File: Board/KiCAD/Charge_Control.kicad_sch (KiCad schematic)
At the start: 57 parts, among them Q1 AON7408, Q10 AON7407, Q2 AON7408, Q3 AON7408, Q4 AON7408, U1 BQ25730RSNR, U3 LTC2943CDD#PBF

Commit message: Edits to PCB
@andrewgreenberg @KeytarGoblin
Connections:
- net GND renamed 33
- net 33: now also U1.33, U1.34, U1.35, U1.36, U1.37, U1.38, U1.39, U1.40, U1.41, U1.42
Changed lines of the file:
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@@
 	)
 	(symbol
-		(lib_name "BQ25730RSNR_1")
 		(lib_id "BQ25730RSNR:BQ25730RSNR")
 		(at 123.19 88.9 0)
@@
 		(pin "27"
 		)
+		(pin "39"
+		)
+		(pin "33"
+		)
+		(pin "40"
+		)
+		(pin "35"
+		)
+		(pin "38"
+		)
+		(pin "36"
+		)
+		(pin "41"
+		)
+		(pin "34"
+		)
+		(pin "37"
+		)
+		(pin "42"
+		)
 		(instances

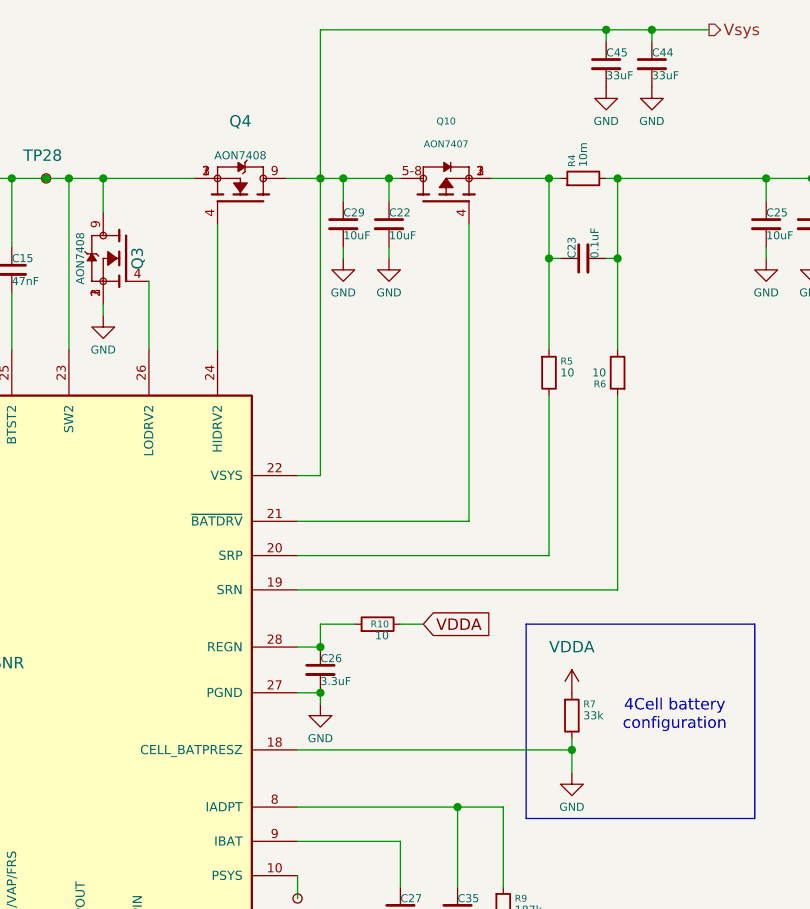
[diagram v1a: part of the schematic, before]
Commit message: Fixed Library paths for component symbol
@andrewgreenberg @KeytarGoblin
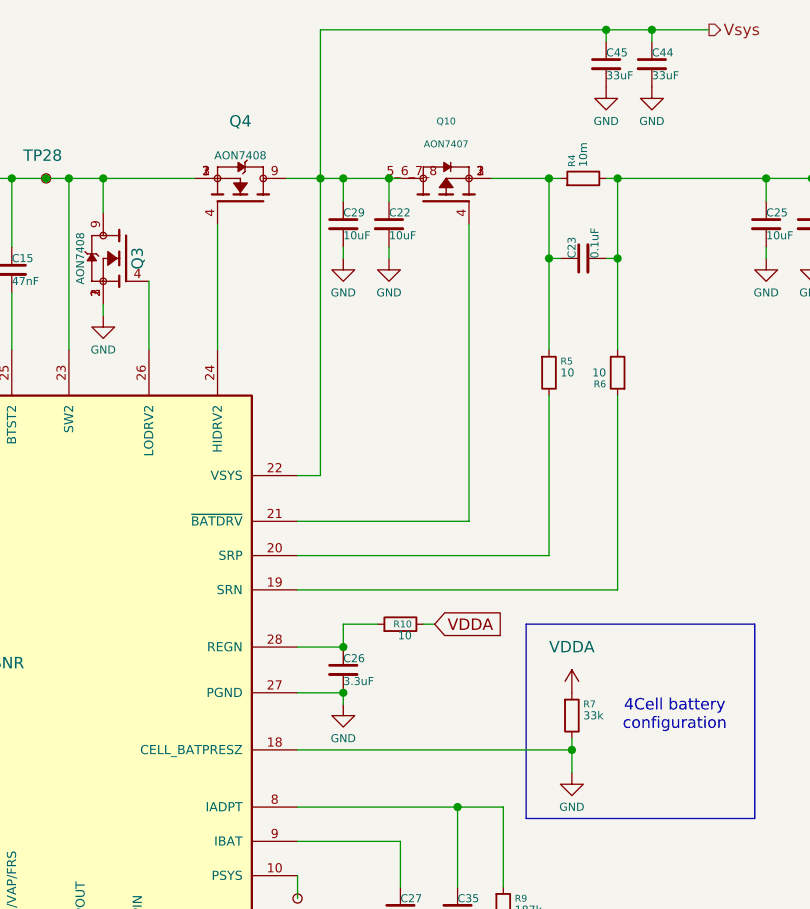
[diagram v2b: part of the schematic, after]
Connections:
- net Vsys: now also Q10.5_6_7_8; no longer Q10.5-8
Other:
- moved on the sheet: C26, Q10, R10
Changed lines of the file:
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@@
 	)
 	(junction
-		(at 162.56 92.71)
+		(at 165.1 92.71)
 		(diameter 0)
 		(color 0 0 0 0)
@@
 	)
 	(junction
-		(at 162.56 87.63)
+		(at 165.1 87.63)
 		(diameter 0)
 		(color 0 0 0 0)
@@
 	(wire
 		(pts
-			(xy 173.99 85.09) (xy 171.45 85.09)
+			(xy 175.26 85.09) (xy 173.99 85.09)
 		)
 		(stroke
@@
 	(wire
 		(pts
-			(xy 162.56 85.09) (xy 162.56 87.63)
+			(xy 165.1 85.09) (xy 165.1 87.63)
 		)
 		(stroke
@@
 	(wire
 		(pts
-			(xy 166.37 85.09) (xy 162.56 85.09)
+			(xy 168.91 85.09) (xy 165.1 85.09)
 		)
 		(stroke
@@
 	(wire
 		(pts
+			(xy 160.02 92.71) (xy 165.1 92.71)
+		)
+		(stroke
+			(width 0)
+			(type default)
+		)
+	)
+	(wire
+		(pts
 			(xy 74.93 62.23) (xy 77.47 62.23)
 		)
@@
 	(wire
 		(pts
-			(xy 160.02 87.63) (xy 162.56 87.63)
-		)
-		(stroke
-			(width 0)
-			(type default)
-		)
-	)
-	(wire
-		(pts
 			(xy 54.61 35.56) (xy 58.42 35.56)
 		)
@@
 	(wire
 		(pts
-			(xy 160.02 92.71) (xy 162.56 92.71)
-		)
-		(stroke
-			(width 0)
-			(type default)
-		)
-	)
-	(wire
-		(pts
 			(xy 162.56 35.56) (xy 165.1 35.56)
 		)
@@
 	(wire
 		(pts
-			(xy 162.56 92.71) (xy 162.56 93.98)
+			(xy 165.1 92.71) (xy 165.1 93.98)
 		)
 		(stroke
@@
 	(wire
 		(pts
+			(xy 160.02 87.63) (xy 165.1 87.63)
+		)
+		(stroke
+			(width 0)
+			(type default)
+		)
+	)
+	(wire
+		(pts
 			(xy 177.8 119.38) (xy 177.8 120.65)
 		)
@@
 	(global_label "VDDA"
 		(shape input)
-		(at 173.99 85.09 0)
+		(at 175.26 85.09 0)
 		(fields_autoplaced yes)
 		(effects
@@
 		)
 		(property "Intersheetrefs" "${INTERSHEET_REFS}"
-			(at 181.6924 85.09 0)
+			(at 182.9624 85.09 0)
 			(effects
 				(font
@@
 	(symbol
 		(lib_id "power:GND")
-		(at 162.56 93.98 0)
+		(at 165.1 93.98 0)
 		(unit 1)
 		(exclude_from_sim no)
@@
 		(dnp no)
 		(property "Reference" "#PWR058"
-			(at 162.56 100.33 0)
+			(at 165.1 100.33 0)
 			(effects
 				(font
@@
 		)
 		(property "Value" "GND"
-			(at 162.56 97.79 0)
+			(at 165.1 97.79 0)
 			(effects
 				(font
@@
 		)
 		(property "Footprint" ""
-			(at 162.56 93.98 0)
+			(at 165.1 93.98 0)
 			(effects
 				(font
@@
 		)
 		(property "Datasheet" ""
-			(at 162.56 93.98 0)
+			(at 165.1 93.98 0)
 			(effects
 				(font
@@
 		)
 		(property "Description" "Power symbol creates a global label with name \"GND\" , ground"
-			(at 162.56 93.98 0)
+			(at 165.1 93.98 0)
 			(effects
 				(font
@@
 	(symbol
 		(lib_id "Device:C_Small")
-		(at 162.56 90.17 0)
+		(at 165.1 90.17 0)
 		(unit 1)
 		(exclude_from_sim no)
@@
 		(dnp no)
 		(property "Reference" "C26"
-			(at 162.56 88.9 0)
+			(at 165.1 88.9 0)
 			(effects
 				(font
@@
 		)
 		(property "Value" "3.3uF"
-			(at 162.56 91.44 0)
+			(at 165.1 91.44 0)
 			(effects
 				(font
@@
 		)
 		(property "Footprint" "Capacitor_SMD:C_0603_1608Metric"
-			(at 162.56 90.17 0)
+			(at 165.1 90.17 0)
 			(effects
 				(font
@@
 		)
 		(property "Datasheet" "~"
-			(at 162.56 90.17 0)
+			(at 165.1 90.17 0)
 			(effects
 				(font
@@
 		)
 		(property "Description" "Unpolarized capacitor, small symbol"
-			(at 162.56 90.17 0)
+			(at 165.1 90.17 0)
 			(effects
 				(font
@@
 		)
 		(property "SNAPEDA_PN" ""
-			(at 162.56 90.17 0)
+			(at 165.1 90.17 0)
 			(effects
 				(font
@@
 		(pin "3"
 		)
-		(pin "5-8"
+		(pin "5_6_7_8"
 		)
 		(pin "4"
@@
 	(symbol
 		(lib_id "Device:R_Small")
-		(at 168.91 85.09 90)
+		(at 171.45 85.09 90)
 		(unit 1)
 		(exclude_from_sim no)
@@
 		(dnp no)
 		(property "Reference" "R10"
-			(at 170.18 85.09 90)
+			(at 172.72 85.09 90)
 			(effects
 				(font
@@
 		)
 		(property "Value" "10"
-			(at 170.18 86.36 90)
+			(at 172.72 86.36 90)
 			(effects
 				(font
@@
 		)
 		(property "Footprint" "Resistor_SMD:R_0603_1608Metric"
-			(at 168.91 85.09 0)
+			(at 171.45 85.09 0)
 			(effects
 				(font
@@
 		)
 		(property "Datasheet" "~"
-			(at 168.91 85.09 0)
+			(at 171.45 85.09 0)
 			(effects
 				(font
@@
 		)
 		(property "Description" "Resistor, small symbol"
-			(at 168.91 85.09 0)
+			(at 171.45 85.09 0)
 			(effects
 				(font
@@
 		)
 		(property "SNAPEDA_PN" ""
-			(at 168.91 85.09 0)
+			(at 171.45 85.09 0)
 			(effects
 				(font

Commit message: PCB Revision
PCN near full completion, currently running on no errors while running DRC.

@KeytarGoblin @andrewgreenberg @Danish2PSU
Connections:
- net Vsys: now also Q10.5-8; no longer Q10.5_6_7_8
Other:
- moved on the sheet: Q10
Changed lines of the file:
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@@
 	)
 	(junction
+		(at 170.18 35.56)
+		(diameter 0)
+		(color 0 0 0 0)
+	)
+	(junction
 		(at 199.39 19.05)
 		(diameter 0)
@@
 	)
 	(junction
-		(at 170.18 35.56)
-		(diameter 0)
-		(color 0 0 0 0)
-	)
-	(junction
 		(at 217.17 35.56)
 		(diameter 0)
@@
 	(wire
 		(pts
+			(xy 171.45 35.56) (xy 170.18 35.56)
+		)
+		(stroke
+			(width 0)
+			(type default)
+		)
+	)
+	(wire
+		(pts
 			(xy 160.02 77.47) (xy 187.96 77.47)
 		)
@@
 	(wire
 		(pts
-			(xy 170.18 35.56) (xy 171.45 35.56)
-		)
-		(stroke
-			(width 0)
-			(type default)
-		)
-	)
-	(wire
-		(pts
 			(xy 67.31 50.8) (xy 67.31 35.56)
 		)
@@
 		(pin "3"
 		)
-		(pin "5_6_7_8"
+		(pin "5-8"
 		)
 		(pin "4"

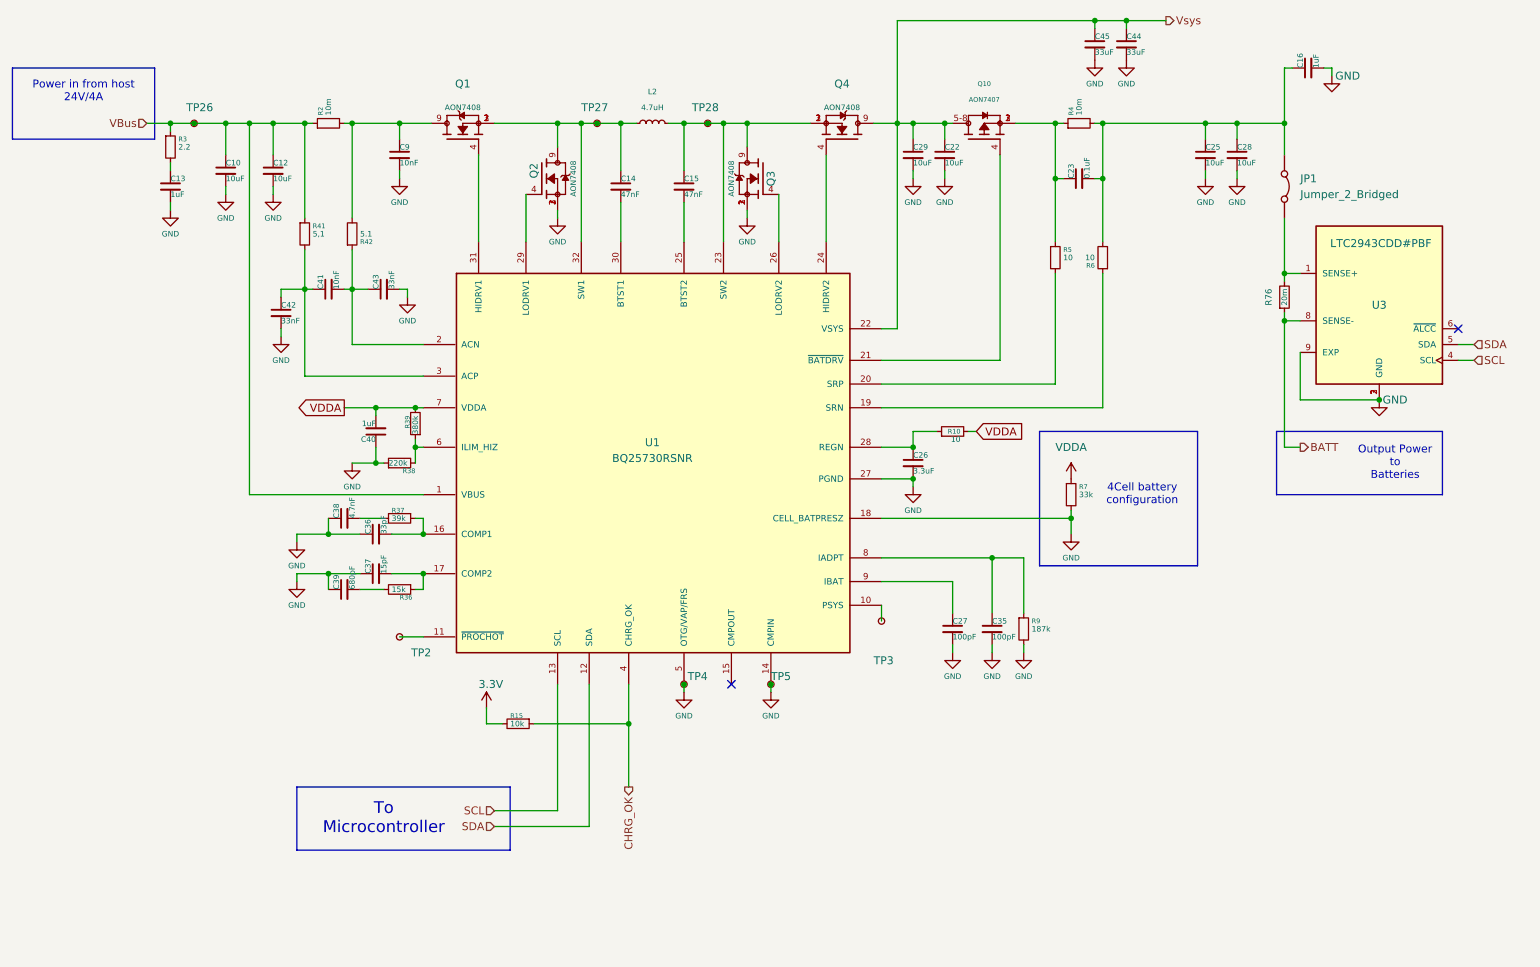
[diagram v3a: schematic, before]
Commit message: Aesthetics edit
@andrewgreenberg
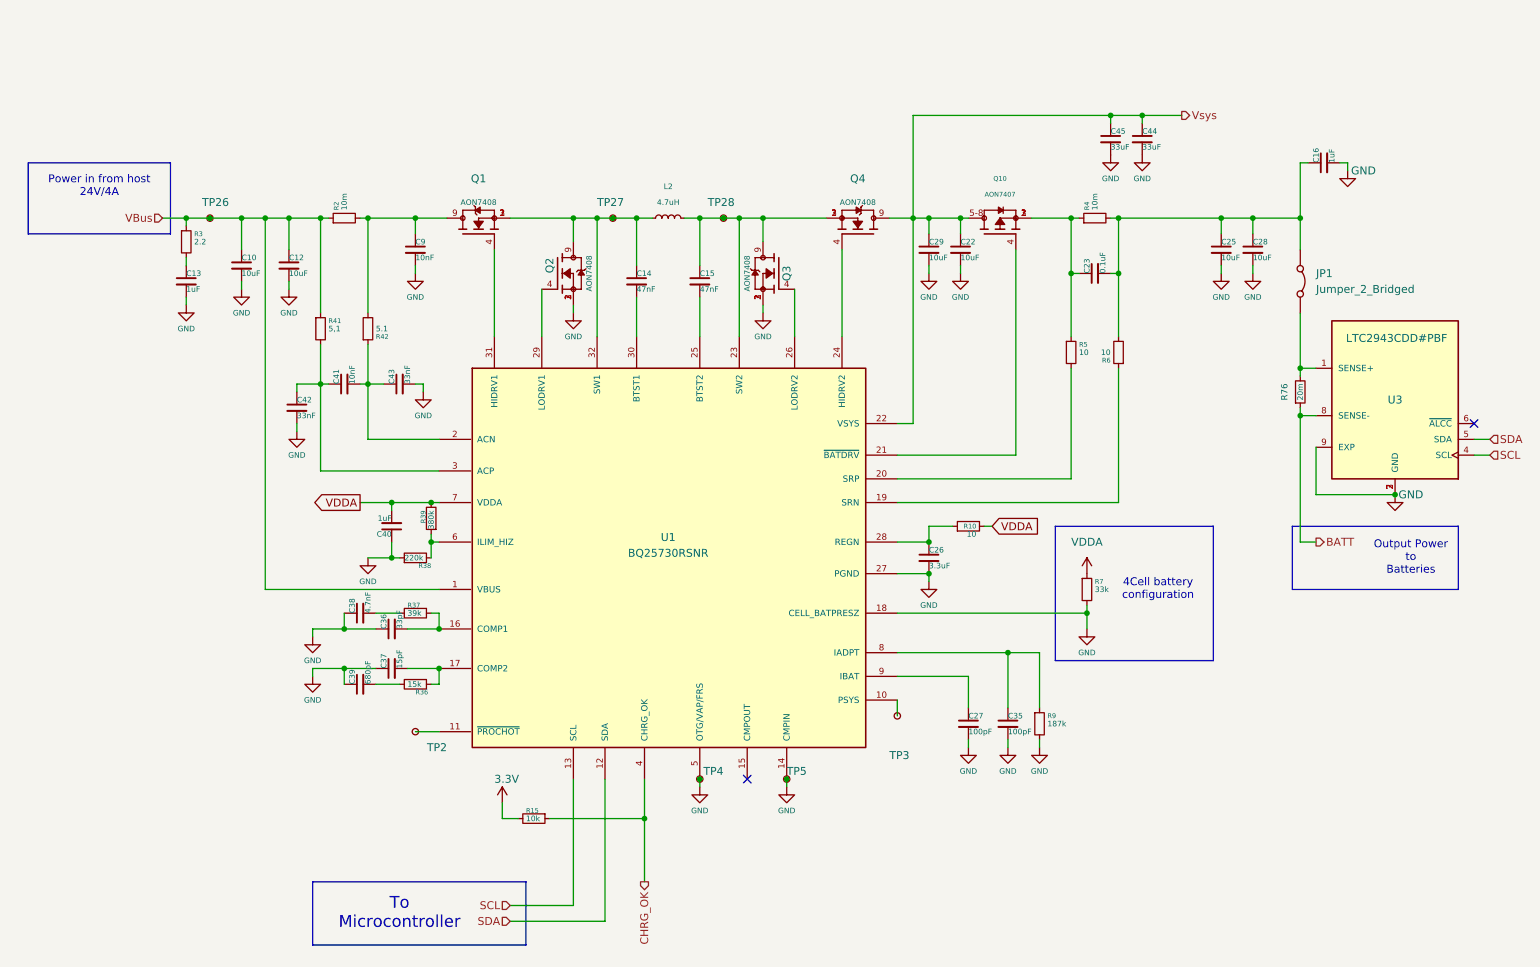
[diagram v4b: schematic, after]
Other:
- moved on the sheet: C10, C12, C13, C14, C15, C16, C22, C23, C25, C26, C27, C28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

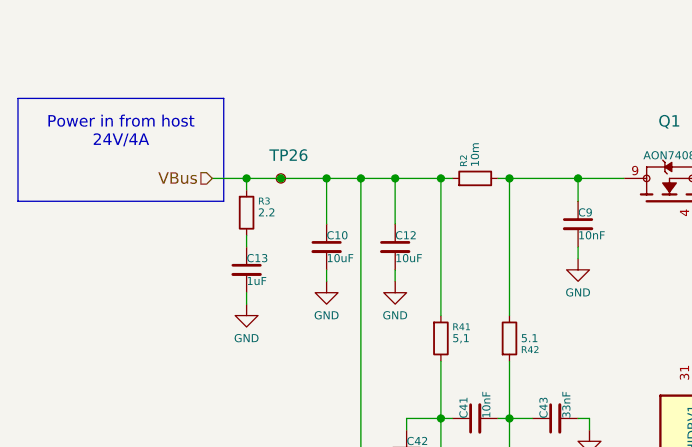
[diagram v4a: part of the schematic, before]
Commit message: Polish on schematic and board. Changed balance resistors to 100 ohms. Lots of silly OCD cleanup and documentation. Board has thicker (0.2mm) I2C lines, cleaned up 3.3V connections to reduce impedance, lots of other small tweaks.
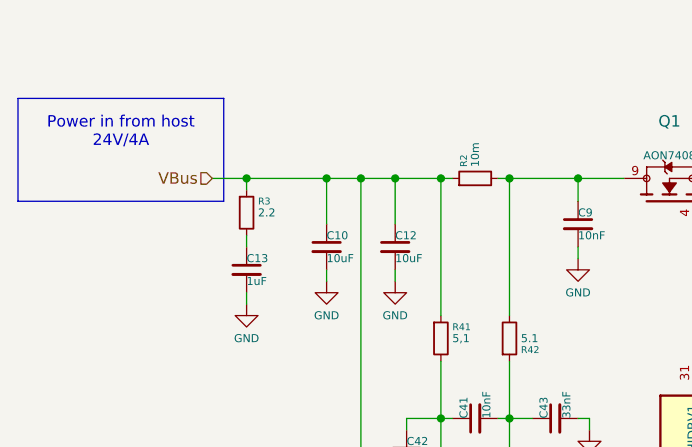
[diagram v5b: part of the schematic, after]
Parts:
- removed TP26: TestPoint_Small, TestPoint:TestPoint_THTPad_1.0x1.0mm_Drill0.5mm, symbol Connector:TestPoint_Small
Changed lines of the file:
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@@
-	)
-	(junction
-		(at 52.07 50.8)
-		(diameter 0)
-		(color 0 0 0 0)
 	)
 	(junction
@@
 	(wire
 		(pts
-			(xy 52.07 50.8) (xy 57.15 50.8)
+			(xy 48.26 50.8) (xy 57.15 50.8)
 		)
 		(stroke
@@
 		(pts
 			(xy 83.82 123.19) (xy 88.9 123.19)
-		)
-		(stroke
-			(width 0)
-			(type default)
-		)
-	)
-	(wire
-		(pts
-			(xy 48.26 50.8) (xy 52.07 50.8)
 		)
 		(stroke
@@
 					(unit 1)
 				)
-			)
-		)
-	)
-	(symbol
-		(lib_id "Connector:TestPoint_Small")
-		(at 52.07 50.8 0)
-		(unit 1)
-		(exclude_from_sim no)
-		(in_bom yes)
-		(on_board yes)
-		(dnp no)
-		(property "Reference" "TP26"
-			(at 50.8 48.26 0)
-			(effects
-				(font
-					(size 1.27 1.27)
-				)
-				(justify left)
-			)
-		)
-		(property "Value" "TestPoint_Small"
-			(at 48.26 46.99 0)
-			(effects
-				(font
-					(size 1.27 1.27)
-				)
-				(justify left)
-				(hide yes)
-			)
-		)
-		(property "Footprint" "TestPoint:TestPoint_THTPad_1.0x1.0mm_Drill0.5mm"
-			(at 57.15 50.8 0)
-			(effects
-				(font
-					(size 1.27 1.27)
-				)
-				(hide yes)
-			)
-		)
-		(property "Datasheet" "~"
-			(at 57.15 50.8 0)
-			(effects
-				(font
-					(size 1.27 1.27)
-				)
-				(hide yes)
-			)
-		)
-		(property "Description" "test point"
-			(at 52.07 50.8 0)
-			(effects
-				(font
-					(size 1.27 1.27)
-				)
-				(hide yes)
-			)
-		)
-		(property "SNAPEDA_PN" ""
-			(at 52.07 50.8 0)
-			(effects
-				(font
-					(size 1.27 1.27)
-				)
-			)
-		)
-		(pin "1"
-		)
-		(instances
-			(project "Battery_Management_System"
-				(path "/1ea1a1f5-2618-4570-85b6-e164c8f0e76f/70546578-20d6-4cac-ac3f-606caa4a96bc"
-					(reference "TP26")
-					(unit 1)
-				)
